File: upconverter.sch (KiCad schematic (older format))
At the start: 28 parts, among them J1 Barrel_Jack, J2 SMA_F, J3 SMA_F, U1 L7805, U2 TPS71533__SC70, U3 SA602A, X1 XO32

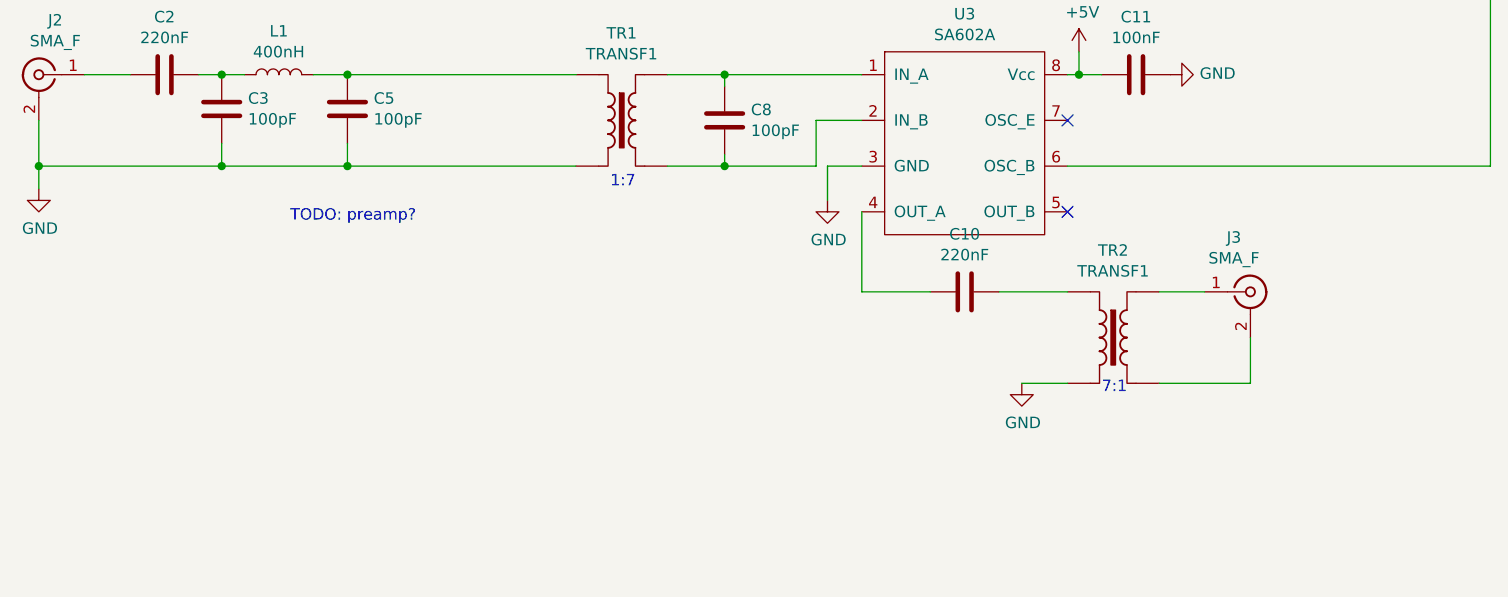
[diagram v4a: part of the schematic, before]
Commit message: started layout, footprints on new changes
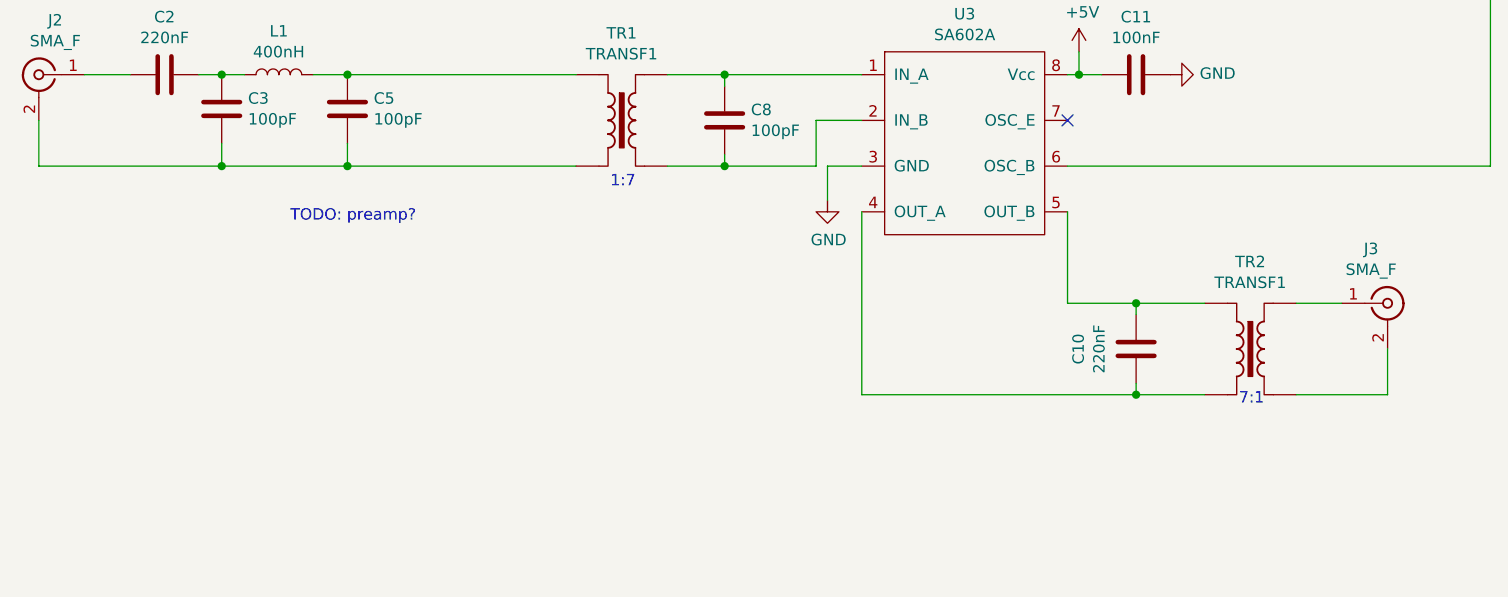
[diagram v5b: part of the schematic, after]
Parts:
- C1: footprint (none) -> Capacitor_SMD:C_0805_2012Metric
- J1: footprint (none) -> ZAM_Custom:PJ-002A_2.1_5.5_Barrel_Jack_CUI
- J2, J3: footprint (none) -> Connector_Coaxial:SMA_Amphenol_901-144_Vertical
- L1: footprint (none) -> Inductor_SMD:L_0805_2012Metric
- TR1, TR2: footprint (none) -> ZAM_Custom:fair-rite_2643625002
- U1: footprint (none) -> Package_TO_SOT_THT:TO-220-3_Vertical
- X1: footprint (none) -> Oscillator:Oscillator_SMD_IDT_JU6-6_7.0x5.0mm_P2.54mm
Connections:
- net GND: no longer C3.2, C5.2, J2.2 (Ext), TR1.2, TR2.2
- net at C10.2, U3.4 (OUT_A): now also TR2.2
- net at U3.5 (OUT_B): now also C10.1, TR2.1
- new net: C3.2, C5.2, J2.2 (Ext), TR1.2
- no-connect marks 2 -> 1
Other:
- moved on the sheet: C10, J3, TR2
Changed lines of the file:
@@
-$EndComp
-$Comp
-L power:GND #PWR03
-U 1 1 5EF7D2F9
-P 4350 4350
-F 0 "#PWR03" H 4350 4100 50  0001 C CNN
-F 1 "GND" H 4355 4177 50  0000 C CNN
-F 2 "" H 4350 4350 50  0001 C CNN
-F 3 "" H 4350 4350 50  0001 C CNN
-	1    4350 4350
-	1    0    0    -1
 $EndComp
 $Comp
@@
 F 0 "L1" V 5590 3850 50  0000 C CNN
 F 1 "400nH" V 5499 3850 50  0000 C CNN
-F 2 "" H 5400 3850 50  0001 C CNN
+F 2 "Inductor_SMD:L_0805_2012Metric" H 5400 3850 50  0001 C CNN
 F 3 "~" H 5400 3850 50  0001 C CNN
 	1    5400 3850
@@
 Wire Wire Line
 	4350 4250 5150 4250
-Wire Wire Line
-	4350 4250 4350 4350
 $Comp
 L Connector:Conn_Coaxial J2
@@
 F 0 "J2" H 4278 4088 50  0000 C CNN
 F 1 "SMA_F" H 4278 3997 50  0000 C CNN
-F 2 "" H 4350 3850 50  0001 C CNN
+F 2 "Connector_Coaxial:SMA_Amphenol_901-144_Vertical" H 4350 3850 50  0001 C CNN
 F 3 " ~" H 4350 3850 50  0001 C CNN
 	1    4350 3850
@@
 Wire Wire Line
 	4350 4050 4350 4250
-Connection ~ 4350 4250
 $Comp
 L Connector:Conn_Coaxial J3
 U 1 1 5EFAC751
-P 9650 4800
-F 0 "J3" H 9578 5038 50  0000 C CNN
-F 1 "SMA_F" H 9578 4947 50  0000 C CNN
-F 2 "" H 9650 4800 50  0001 C CNN
-F 3 " ~" H 9650 4800 50  0001 C CNN
-	1    9650 4800
-	1    0    0    -1
-$EndComp
-Wire Wire Line
-	7950 4450 7950 4800
+P 10250 4850
+F 0 "J3" H 10178 5088 50  0000 C CNN
+F 1 "SMA_F" H 10178 4997 50  0000 C CNN
+F 2 "Connector_Coaxial:SMA_Amphenol_901-144_Vertical" H 10250 4850 50  0001 C CNN
+F 3 " ~" H 10250 4850 50  0001 C CNN
+	1    10250 4850
+	1    0    0    -1
+$EndComp
 Wire Wire Line
 	8900 3850 8850 3850
@@
 F 0 "X1" H 8094 2646 50  0000 L CNN
 F 1 "XO32" H 8094 2555 50  0000 L CNN
-F 2 "" H 8450 2250 50  0001 C CNN
+F 2 "Oscillator:Oscillator_SMD_IDT_JU6-6_7.0x5.0mm_P2.54mm" H 8450 2250 50  0001 C CNN
 F 3 "http://cdn-reichelt.de/documents/datenblatt/B400/XO32.pdf" H 7650 2600 50  0001 C CNN
 	1    7750 2600
@@
 Wire Wire Line
 	9450 2900 9700 2900
-NoConn ~ 8850 4450
 $Comp
 L Connector:Barrel_Jack J1
@@
 F 0 "J1" H 5707 7325 50  0000 C CNN
 F 1 "Barrel_Jack" H 5707 7234 50  0000 C CNN
-F 2 "" H 5700 6960 50  0001 C CNN
+F 2 "ZAM_Custom:PJ-002A_2.1_5.5_Barrel_Jack_CUI" H 5700 6960 50  0001 C CNN
 F 3 "~" H 5700 6960 50  0001 C CNN
 	1    5650 7000
@@
 F 0 "TR1" H 6900 4431 50  0000 C CNN
 F 1 "TRANSF1" H 6900 4340 50  0000 C CNN
-F 2 "" H 6900 4050 50  0001 C CNN
+F 2 "ZAM_Custom:fair-rite_2643625002" H 6900 4050 50  0001 C CNN
 F 3 "" H 6900 4050 50  0001 C CNN
 	1    6900 4050
@@
 L Transformer:TRANSF1 TR2
 U 1 1 60F90E80
-P 9050 5000
-F 0 "TR2" H 9050 5381 50  0000 C CNN
-F 1 "TRANSF1" H 9050 5290 50  0000 C CNN
-F 2 "" H 9050 5000 50  0001 C CNN
-F 3 "" H 9050 5000 50  0001 C CNN
-	1    9050 5000
-	1    0    0    -1
-$EndComp
-$Comp
-L power:GND #PWR09
-U 1 1 60F990B0
-P 8650 5200
-F 0 "#PWR09" H 8650 4950 50  0001 C CNN
-F 1 "GND" H 8655 5027 50  0000 C CNN
-F 2 "" H 8650 5200 50  0001 C CNN
-F 3 "" H 8650 5200 50  0001 C CNN
-	1    8650 5200
+P 9650 5050
+F 0 "TR2" H 9650 5431 50  0000 C CNN
+F 1 "TRANSF1" H 9650 5340 50  0000 C CNN
+F 2 "ZAM_Custom:fair-rite_2643625002" H 9650 5050 50  0001 C CNN
+F 3 "" H 9650 5050 50  0001 C CNN
+	1    9650 5050
 	1    0    0    -1
 $EndComp
@@
 L Device:C C10
 U 1 1 60F9E5B1
-P 8400 4800
-F 0 "C10" V 8148 4800 50  0000 C CNN
-F 1 "220nF" V 8239 4800 50  0000 C CNN
-F 2 "Capacitor_SMD:C_0805_2012Metric" H 8438 4650 50  0001 C CNN
-F 3 "~" H 8400 4800 50  0001 C CNN
-	1    8400 4800
-	0    1    1    0
-$EndComp
-Wire Wire Line
-	8550 4800 8850 4800
-Wire Wire Line
-	8250 4800 7950 4800
-Wire Wire Line
-	9250 4800 9450 4800
+P 9150 5050
+F 0 "C10" V 8898 5050 50  0000 C CNN
+F 1 "220nF" V 8989 5050 50  0000 C CNN
+F 2 "Capacitor_SMD:C_0805_2012Metric" H 9188 4900 50  0001 C CNN
+F 3 "~" H 9150 5050 50  0001 C CNN
+	1    9150 5050
+	1    0    0    -1
+$EndComp
+Wire Wire Line
+	9150 4850 9450 4850
+Wire Wire Line
+	9850 4850 10050 4850
 Wire Wire Line
 	5950 6900 6350 6900
@@
 F 0 "C1" H 6915 7146 50  0000 L CNN
 F 1 "10uF" H 6915 7055 50  0000 L CNN
-F 2 "" H 6800 7100 50  0001 C CNN
+F 2 "Capacitor_SMD:C_0805_2012Metric" H 6800 7100 50  0001 C CNN
 F 3 "~" H 6800 7100 50  0001 C CNN
 	1    6800 7100
@@
 F 0 "U1" H 7600 7142 50  0000 C CNN
 F 1 "L7805" H 7600 7051 50  0000 C CNN
-F 2 "" H 7625 6750 50  0001 L CIN
+F 2 "Package_TO_SOT_THT:TO-220-3_Vertical" H 7625 6750 50  0001 L CIN
 F 3 "http://www.st.com/content/ccc/resource/technical/document/datasheet/41/4f/b3/b0/12/d4/47/88/CD00000444.pdf/files/CD00000444.pdf/jcr:content/translations/en.CD00000444.pdf" H 7600 6850 50  0001 C CNN
 	1    7600 6900
@@
 Text Notes 6850 4350 0    50   ~ 0
 1:7
-Text Notes 9000 5250 0    50   ~ 0
+Text Notes 9600 5300 0    50   ~ 0
 7:1
 Text Notes 5450 4500 0    50   ~ 0
 TODO: preamp?
 Wire Wire Line
-	8650 5200 8850 5200
-Wire Wire Line
-	9650 5000 9650 5200
-Wire Wire Line
-	9650 5200 9250 5200
+	10250 5050 10250 5250
+Wire Wire Line
+	10250 5250 9850 5250
+Wire Wire Line
+	9150 5250 9150 5200
+Wire Wire Line
+	9150 5250 9450 5250
+Connection ~ 9150 5250
+Wire Wire Line
+	7950 5250 9150 5250
+Wire Wire Line
+	7950 4450 7950 5250
+Wire Wire Line
+	9150 4900 9150 4850
+Wire Wire Line
+	9150 4850 8850 4850
+Wire Wire Line
+	8850 4850 8850 4450
+Connection ~ 9150 4850
 $EndSCHEMATC

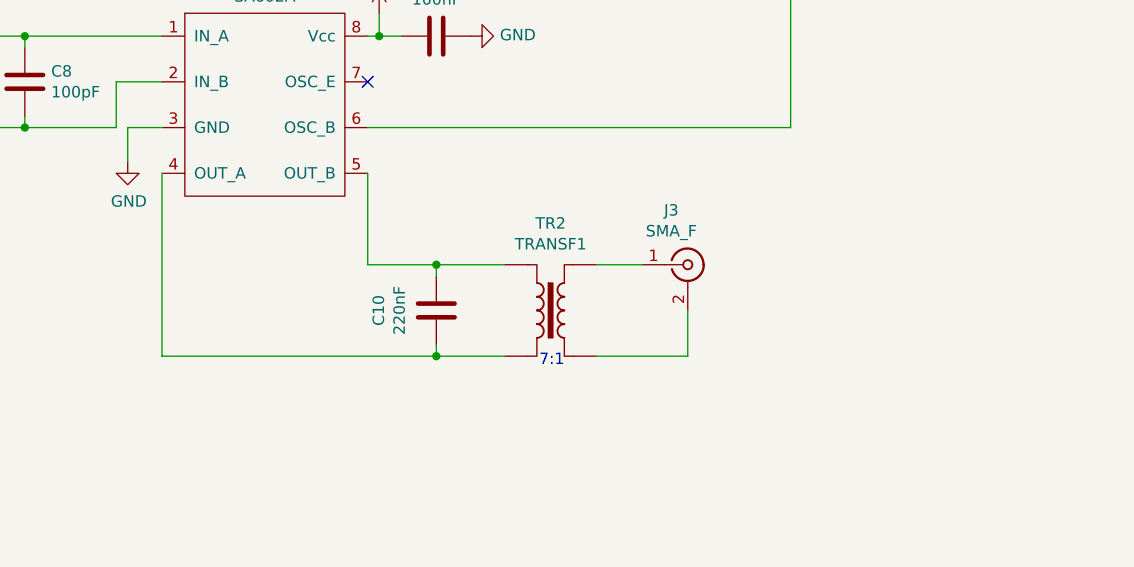
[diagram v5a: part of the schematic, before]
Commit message: Updated output filter
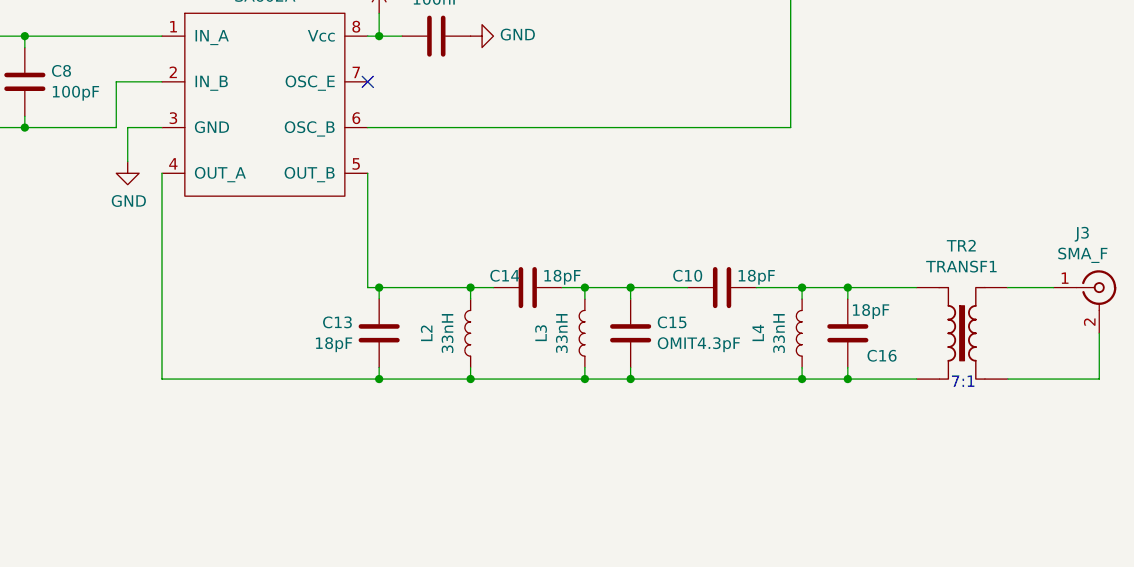
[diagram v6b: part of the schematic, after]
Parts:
- added C13, C14: 18pF, Capacitor_SMD:C_0603_1608Metric, symbol Device:C
- added C15: OMIT4.3pF, Capacitor_SMD:C_0603_1608Metric, symbol Device:C
- added C16: 18pF, Capacitor_SMD:C_0805_2012Metric, symbol Device:C
- added L2, L3, L4: 33nH, Inductor_SMD:L_0805_2012Metric, symbol Device:L
- C10: value 220nF -> 18pF
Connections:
- net at TR2.2, U3.4 (OUT_A): now also C13.1, C15.2, C16.1, L2.1, L3.1, L4.1; no longer C10.2
- new net: C13.2, C14.2, L2.2, U3.5 (OUT_B)
- new net: C10.2, C16.2, L4.2, TR2.1
- new net: C10.1, C14.1, C15.1, L3.2
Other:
- moved on the sheet: C10, J3, TR2
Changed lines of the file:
@@
 L Connector:Conn_Coaxial J3
 U 1 1 5EFAC751
-P 10250 4850
-F 0 "J3" H 10178 5088 50  0000 C CNN
-F 1 "SMA_F" H 10178 4997 50  0000 C CNN
-F 2 "Connector_Coaxial:SMA_Amphenol_901-144_Vertical" H 10250 4850 50  0001 C CNN
-F 3 " ~" H 10250 4850 50  0001 C CNN
-	1    10250 4850
+P 12050 4950
+F 0 "J3" H 11978 5188 50  0000 C CNN
+F 1 "SMA_F" H 11978 5097 50  0000 C CNN
+F 2 "Connector_Coaxial:SMA_Amphenol_901-144_Vertical" H 12050 4950 50  0001 C CNN
+F 3 " ~" H 12050 4950 50  0001 C CNN
+	1    12050 4950
 	1    0    0    -1
 $EndComp
@@
 	-1   0    0    1
 $EndComp
-$Comp
-L Transformer:TRANSF1 TR1
-U 1 1 60F79481
-P 6900 4050
-F 0 "TR1" H 6900 4431 50  0000 C CNN
-F 1 "TRANSF1" H 6900 4340 50  0000 C CNN
-F 2 "ZAM_Custom:fair-rite_2643625002" H 6900 4050 50  0001 C CNN
-F 3 "" H 6900 4050 50  0001 C CNN
-	1    6900 4050
-	1    0    0    -1
-$EndComp
 Wire Wire Line
 	5700 3850 6700 3850
@@
 L Transformer:TRANSF1 TR2
 U 1 1 60F90E80
-P 9650 5050
-F 0 "TR2" H 9650 5431 50  0000 C CNN
-F 1 "TRANSF1" H 9650 5340 50  0000 C CNN
-F 2 "ZAM_Custom:fair-rite_2643625002" H 9650 5050 50  0001 C CNN
-F 3 "" H 9650 5050 50  0001 C CNN
-	1    9650 5050
+P 11450 5150
+F 0 "TR2" H 11450 5531 50  0000 C CNN
+F 1 "TRANSF1" H 11450 5440 50  0000 C CNN
+F 2 "ZAM_Custom:fair-rite_2643625002" H 11450 5150 50  0001 C CNN
+F 3 "" H 11450 5150 50  0001 C CNN
+	1    11450 5150
 	1    0    0    -1
 $EndComp
@@
 L Device:C C10
 U 1 1 60F9E5B1
-P 9150 5050
-F 0 "C10" V 8898 5050 50  0000 C CNN
-F 1 "220nF" V 8989 5050 50  0000 C CNN
-F 2 "Capacitor_SMD:C_0805_2012Metric" H 9188 4900 50  0001 C CNN
-F 3 "~" H 9150 5050 50  0001 C CNN
-	1    9150 5050
-	1    0    0    -1
-$EndComp
-Wire Wire Line
-	9150 4850 9450 4850
-Wire Wire Line
-	9850 4850 10050 4850
+P 10400 4950
+F 0 "C10" V 10450 5100 50  0000 C CNN
+F 1 "18pF" V 10450 4800 50  0000 C CNN
+F 2 "Capacitor_SMD:C_0805_2012Metric" H 10438 4800 50  0001 C CNN
+F 3 "~" H 10400 4950 50  0001 C CNN
+	1    10400 4950
+	0    -1   -1   0
+$EndComp
+Wire Wire Line
+	10950 4950 11250 4950
+Wire Wire Line
+	11650 4950 11850 4950
 Wire Wire Line
 	5950 6900 6350 6900
@@
 Wire Wire Line
 	7800 4250 7800 4400
-Text Notes 6850 4350 0    50   ~ 0
-1:7
-Text Notes 9600 5300 0    50   ~ 0
+Text Notes 11400 5400 0    50   ~ 0
 7:1
 Text Notes 5450 4500 0    50   ~ 0
 TODO: preamp?
 Wire Wire Line
-	10250 5050 10250 5250
-Wire Wire Line
-	10250 5250 9850 5250
-Wire Wire Line
-	9150 5250 9150 5200
-Wire Wire Line
-	9150 5250 9450 5250
-Connection ~ 9150 5250
-Wire Wire Line
-	7950 5250 9150 5250
-Wire Wire Line
-	7950 4450 7950 5250
-Wire Wire Line
-	9150 4900 9150 4850
-Wire Wire Line
-	9150 4850 8850 4850
-Wire Wire Line
-	8850 4850 8850 4450
-Connection ~ 9150 4850
+	12050 5150 12050 5350
+Wire Wire Line
+	12050 5350 11650 5350
+Wire Wire Line
+	10950 5350 10950 5300
+Wire Wire Line
+	10950 5350 11250 5350
+Connection ~ 10950 5350
+Wire Wire Line
+	10950 5000 10950 4950
+$Comp
+L Device:L L4
+U 1 1 60F8630A
+P 10750 5150
+F 0 "L4" V 10940 5150 50  0000 C CNN
+F 1 "33nH" V 10849 5150 50  0000 C CNN
+F 2 "Inductor_SMD:L_0805_2012Metric" H 10750 5150 50  0001 C CNN
+F 3 "~" H 10750 5150 50  0001 C CNN
+	1    10750 5150
+	-1   0    0    1
+$EndComp
+$Comp
+L Device:C C15
+U 1 1 60F8754D
+P 10000 5150
+F 0 "C15" H 10115 5196 50  0000 L CNN
+F 1 "OMIT4.3pF" H 10115 5105 50  0000 L CNN
+F 2 "Capacitor_SMD:C_0603_1608Metric" H 10038 5000 50  0001 C CNN
+F 3 "~" H 10000 5150 50  0001 C CNN
+	1    10000 5150
+	1    0    0    -1
+$EndComp
+Wire Wire Line
+	10000 4950 10000 5000
+Wire Wire Line
+	10000 5300 10000 5350
+Connection ~ 10000 5350
+Wire Wire Line
+	10000 5350 10750 5350
+Wire Wire Line
+	10000 4950 9800 4950
+Connection ~ 10000 4950
+$Comp
+L Device:C C14
+U 1 1 60F97BD9
+P 9550 4950
+F 0 "C14" V 9500 4850 50  0000 C CNN
+F 1 "18pF" V 9500 5100 50  0000 C CNN
+F 2 "Capacitor_SMD:C_0603_1608Metric" H 9588 4800 50  0001 C CNN
+F 3 "~" H 9550 4950 50  0001 C CNN
+	1    9550 4950
+	0    1    1    0
+$EndComp
+$Comp
+L Device:L L2
+U 1 1 60F9F8BE
+P 9300 5150
+F 0 "L2" V 9490 5150 50  0000 C CNN
+F 1 "33nH" V 9399 5150 50  0000 C CNN
+F 2 "Inductor_SMD:L_0805_2012Metric" H 9300 5150 50  0001 C CNN
+F 3 "~" H 9300 5150 50  0001 C CNN
+	1    9300 5150
+	-1   0    0    1
+$EndComp
+Wire Wire Line
+	9400 4950 9300 4950
+Wire Wire Line
+	9300 4950 9300 5000
+Wire Wire Line
+	9300 5300 9300 5350
+Connection ~ 9300 5350
+Wire Wire Line
+	9300 5350 9800 5350
+$Comp
+L Device:C C13
+U 1 1 60FA5B8C
+P 8900 5150
+F 0 "C13" H 8786 5104 50  0000 R CNN
+F 1 "18pF" H 8786 5195 50  0000 R CNN
+F 2 "Capacitor_SMD:C_0603_1608Metric" H 8938 5000 50  0001 C CNN
+F 3 "~" H 8900 5150 50  0001 C CNN
+	1    8900 5150
+	1    0    0    1
+$EndComp
+Connection ~ 9300 4950
+Wire Wire Line
+	8850 4450 8850 4950
+Wire Wire Line
+	7950 5350 8900 5350
+Wire Wire Line
+	7950 4450 7950 5350
+$Comp
+L Device:L L3
+U 1 1 60FAE8DB
+P 9800 5150
+F 0 "L3" V 9990 5150 50  0000 C CNN
+F 1 "33nH" V 9899 5150 50  0000 C CNN
+F 2 "Inductor_SMD:L_0805_2012Metric" H 9800 5150 50  0001 C CNN
+F 3 "~" H 9800 5150 50  0001 C CNN
+	1    9800 5150
+	-1   0    0    1
+$EndComp
+Wire Wire Line
+	8900 5000 8900 4950
+Connection ~ 8900 4950
+Wire Wire Line
+	8900 4950 8850 4950
+Wire Wire Line
+	8900 4950 9300 4950
+Wire Wire Line
+	8900 5300 8900 5350
+Connection ~ 8900 5350
+Wire Wire Line
+	8900 5350 9300 5350
+Wire Wire Line
+	9800 5000 9800 4950
+Connection ~ 9800 4950
+Wire Wire Line
+	9800 4950 9700 4950
+Wire Wire Line
+	9800 5300 9800 5350
+Connection ~ 9800 5350
+Wire Wire Line
+	9800 5350 10000 5350
+Wire Wire Line
+	10000 4950 10250 4950
+Wire Wire Line
+	10550 4950 10750 4950
+Wire Wire Line
+	10750 4950 10750 5000
+Wire Wire Line
+	10750 5300 10750 5350
+Connection ~ 10750 5350
+Wire Wire Line
+	10750 5350 10950 5350
+$Comp
+L Device:C C16
+U 1 1 60FD7697
+P 10950 5150
+F 0 "C16" H 10800 5250 50  0000 C CNN
+F 1 "18pF" H 10850 5050 50  0000 C CNN
+F 2 "Capacitor_SMD:C_0805_2012Metric" H 10988 5000 50  0001 C CNN
+F 3 "~" H 10950 5150 50  0001 C CNN
+	1    10950 5150
+	-1   0    0    1
+$EndComp
+Wire Wire Line
+	10950 4950 10750 4950
+Connection ~ 10950 4950
+Connection ~ 10750 4950
+Text Notes 6850 4350 0    50   ~ 0
+1:7
+$Comp
+L Transformer:TRANSF1 TR1
+U 1 1 60F79481
+P 6900 4050
+F 0 "TR1" H 6900 4431 50  0000 C CNN
+F 1 "TRANSF1" H 6900 4340 50  0000 C CNN
+F 2 "ZAM_Custom:fair-rite_2643625002" H 6900 4050 50  0001 C CNN
+F 3 "" H 6900 4050 50  0001 C CNN
+	1    6900 4050
+	1    0    0    -1
+$EndComp
 $EndSCHEMATC
